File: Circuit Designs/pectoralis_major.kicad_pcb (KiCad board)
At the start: 2 copper layers, 11 x 7.2 mm, 11 parts

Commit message: done all the packages and migrations. Now, time to start to route the module
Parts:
- removed REF** (x3): R-0402, CoF_Resistor:R-0402
- removed REF** (x2): R-0805, CoF_Resistor:R-0805
- removed REF** (x4): C-0402, CoF_Capacitor:C-0402
- removed REF** (x2): C-0805, CoF_Capacitor:C-0805
- added C1: 22uF, CoF_Capacitor:C-0805, F.Cu at (109.1, 60.8)
- added C10: 22uF, CoF_Capacitor:C-0805, F.Cu at (128.1, 49.6)
- added C100: 1uF, CoF_Capacitor:C-0402, F.Cu at (83.8, 33.8)
- added C101: 1uF, CoF_Capacitor:C-0402, F.Cu at (78.4, 40.0)
- added C102: 1uF, CoF_Capacitor:C-0402, F.Cu at (96.5, 22.1)
- added C103: 1uF, CoF_Capacitor:C-0402, F.Cu at (99.2, 20.3)
- added C104: 1uF, CoF_Capacitor:C-0402, F.Cu at (75.7, 43.6)
- added C105: 100nF, CoF_Capacitor:C-0402, F.Cu at (86.5, 33.8)
- added C106: 100nF, CoF_Capacitor:C-0402, F.Cu at (85.6, 30.2)
- added C107: 100nF, CoF_Capacitor:C-0402, F.Cu at (85.6, 28.4)
- added C108: 100nF, CoF_Capacitor:C-0402, F.Cu at (93.7, 20.3)
- added C109: 100pF, CoF_Capacitor:C-0402, F.Cu at (83.0, 24.7)
- added C11: 22uF, CoF_Capacitor:C-0805, F.Cu at (117.5, 60.8)
- added C110: 100nF, CoF_Capacitor:C-0402, F.Cu at (95.0, 25.8)
- added C111: 100pF, CoF_Capacitor:C-0402, F.Cu at (76.0, 27.2)
- added C112: 100pF, CoF_Capacitor:C-0402, F.Cu at (85.6, 20.3)
- added C113: 100pF, CoF_Capacitor:C-0402, F.Cu at (74.8, 30.9)
- added C114: 22uF, CoF_Capacitor:C-0805, F.Cu at (75.3, 63.5)
- added C115: 22uF, CoF_Capacitor:C-0805, F.Cu at (75.3, 60.8)
- added C116: 22uF, CoF_Capacitor:C-0805, F.Cu at (88.3, 49.6)
- added C117: 22uF, CoF_Capacitor:C-0805, F.Cu at (82.7, 54.9)
- added C118: 22uF, CoF_Capacitor:C-0805, F.Cu at (69.9, 66.7)
- added C119: 22uF, CoF_Capacitor:C-0805, F.Cu at (84.1, 52.2)
- added C12: 22uF, CoF_Capacitor:C-0805, F.Cu at (113.1, 66.0)
- added C120: 22uF, CoF_Capacitor:C-0805, F.Cu at (71.1, 63.4)
- added C121: 22uF, CoF_Capacitor:C-0805, F.Cu at (78.5, 54.9)
- added C122: 22uF, CoF_Capacitor:C-0805, F.Cu at (84.1, 49.6)
- added C123: 22uF, CoF_Capacitor:C-0805, F.Cu at (65.7, 68.7)
- added C124: 22uF, CoF_Capacitor:C-0805, F.Cu at (74.2, 58.2)
- added C125: 22uF, CoF_Capacitor:C-0805, F.Cu at (79.9, 49.6)
- added C126: 22uF, CoF_Capacitor:C-0805, F.Cu at (88.3, 52.2)
- added C127: 22uF, CoF_Capacitor:C-0805, F.Cu at (61.5, 69.0)
- added C128: 22uF, CoF_Capacitor:C-0805, F.Cu at (74.2, 53.0)
- added C129: 22uF, CoF_Capacitor:C-0805, F.Cu at (70.0, 55.2)
- added C13: 22uF, CoF_Capacitor:C-0805, F.Cu at (124.0, 54.9)
- added C130: 22uF, CoF_Capacitor:C-0805, F.Cu at (62.6, 66.0)
- added C131: 22uF, CoF_Capacitor:C-0805, F.Cu at (70.0, 52.5)
- added C132: 22uF, CoF_Capacitor:C-0805, F.Cu at (70.0, 57.8)
- added C133: 22uF, CoF_Capacitor:C-0805, F.Cu at (67.9, 60.8)
- added C134: 22uF, CoF_Capacitor:C-0805, F.Cu at (66.8, 64.1)
- added C135: 22uF, CoF_Capacitor:C-0805, F.Cu at (79.9, 52.2)
- added C136: 22uF, CoF_Capacitor:C-0805, F.Cu at (78.5, 57.5)
- added C137: 22uF, CoF_Capacitor:C-0805, F.Cu at (74.2, 55.6)
- added C138: 100nF, CoF_Capacitor:C-0402, F.Cu at (84.2, 60.7)
- added C139: 1uF, CoF_Capacitor:C-0402, F.Cu at (75.8, 69.3)
- added C14: 22uF, CoF_Capacitor:C-0805, F.Cu at (128.1, 52.2)
- added C140: 100nF, CoF_Capacitor:C-0402, F.Cu at (84.6, 58.9)
- added C141: 1uF, CoF_Capacitor:C-0402, F.Cu at (91.8, 51.0)
- added C142: 100nF, CoF_Capacitor:C-0402, F.Cu at (78.8, 61.5)
- added C143: 1uF, CoF_Capacitor:C-0402, F.Cu at (86.1, 54.5)
- added C144: 1uF, CoF_Capacitor:C-0402, F.Cu at (91.8, 52.9)
- added C145: 100nF, CoF_Capacitor:C-0402, F.Cu at (87.4, 56.3)
- added C146: 1uF, CoF_Capacitor:C-0402, F.Cu at (70.4, 70.8)
- added C147: 100nF, CoF_Capacitor:C-0402, F.Cu at (84.6, 57.1)
- added C148: 1uF, CoF_Capacitor:C-0402, F.Cu at (64.9, 70.9)
- added C149: 100nF, CoF_Capacitor:C-0402, F.Cu at (62.8, 63.7)
- added C15: 22uF, CoF_Capacitor:C-0805, F.Cu at (117.3, 63.4)
- added C150: 1nF, CoF_Capacitor:C-0402, F.Cu at (81.5, 62.5)
- added C151: 1nF, CoF_Capacitor:C-0402, F.Cu at (76.1, 65.7)
- added C152: 1nF, CoF_Capacitor:C-0402, F.Cu at (66.1, 66.3)
- added C153: 100nF, CoF_Capacitor:C-0402, F.Cu at (78.8, 67.0)
- added C154: 1uF, CoF_Capacitor:C-0402, F.Cu at (148.9, 48.0)
- added C155: 1uF, CoF_Capacitor:C-0402, F.Cu at (143.6, 54.3)
- added C156: 100nF, CoF_Capacitor:C-0402, F.Cu at (140.8, 56.1)
- added C157: 100nF, CoF_Capacitor:C-0402, F.Cu at (146.3, 52.5)
- added C16: 22uF, CoF_Capacitor:C-0805, F.Cu at (132.3, 49.6)
- added C17: 22uF, CoF_Capacitor:C-0805, F.Cu at (124.0, 57.5)
- added C18: 22uF, CoF_Capacitor:C-0805, F.Cu at (121.8, 60.1)
- added C19: 22uF, CoF_Capacitor:C-0805, F.Cu at (117.3, 66.0)
- added C2: 22uF, CoF_Capacitor:C-0805, F.Cu at (108.9, 63.5)
- added C20: 22uF, CoF_Capacitor:C-0805, F.Cu at (128.2, 54.9)
- added C21: 1uF, CoF_Capacitor:C-0402, F.Cu at (131.6, 51.9)
- added C22: 1uF, CoF_Capacitor:C-0402, F.Cu at (121.0, 62.3)
- added C23: 1uF, CoF_Capacitor:C-0402, F.Cu at (127.4, 57.1)
- added C24: 1uF, CoF_Capacitor:C-0402, F.Cu at (125.2, 59.7)
- added C25: 1uF, CoF_Capacitor:C-0402, F.Cu at (120.8, 64.2)
- added C26: 1uF, CoF_Capacitor:C-0402, F.Cu at (123.7, 62.3)
- added C27: 1uF, CoF_Capacitor:C-0402, F.Cu at (154.7, 23.9)
- added C28: 1uF, CoF_Capacitor:C-0402, F.Cu at (156.9, 22.1)
- added C29: 1uF, CoF_Capacitor:C-0402, F.Cu at (159.6, 20.3)
- added C3: 22uF, CoF_Capacitor:C-0805, F.Cu at (118.5, 53.5)
- added C30: 1uF, CoF_Capacitor:C-0402, F.Cu at (154.7, 25.8)
- added C31: 1uF, CoF_Capacitor:C-0402, F.Cu at (157.4, 23.9)
- added C32: 1uF, CoF_Capacitor:C-0402, F.Cu at (159.6, 22.1)
- added C33: 100nF, CoF_Capacitor:C-0402, F.Cu at (156.9, 20.3)
- added C34: 100nF, CoF_Capacitor:C-0402, F.Cu at (136.0, 23.9)
- added C35: 100nF, CoF_Capacitor:C-0402, F.Cu at (122.9, 31.9)
- added C36: 100nF, CoF_Capacitor:C-0402, F.Cu at (126.6, 32.2)
- added C37: 100nF, CoF_Capacitor:C-0402, F.Cu at (126.4, 26.8)
- added C38: 100nF, CoF_Capacitor:C-0402, F.Cu at (130.5, 22.4)
- added C39: 100nF, CoF_Capacitor:C-0402, F.Cu at (113.1, 40.7)
- added C4: 22uF, CoF_Capacitor:C-0805, F.Cu at (123.9, 49.6)
- added C40: 100nF, CoF_Capacitor:C-0402, F.Cu at (130.5, 24.3)
- added C41: 100nF, CoF_Capacitor:C-0402, F.Cu at (126.4, 28.6)
- added C42: 100nF, CoF_Capacitor:C-0402, F.Cu at (121.1, 34.1)
- added C43: 100nF, CoF_Capacitor:C-0402, F.Cu at (116.6, 38.5)
- added C44: 100nF, CoF_Capacitor:C-0402, F.Cu at (134.3, 20.3)
- added C45: 100nF, CoF_Capacitor:C-0402, F.Cu at (129.1, 26.8)
- added C46: 100nF, CoF_Capacitor:C-0402, F.Cu at (133.2, 22.4)
- added C47: 100nF, CoF_Capacitor:C-0402, F.Cu at (120.4, 36.4)
- added C48: 100nF, CoF_Capacitor:C-0402, F.Cu at (126.4, 30.4)
- added C49: 100nF, CoF_Capacitor:C-0402, F.Cu at (115.8, 40.7)
- added C5: 22uF, CoF_Capacitor:C-0805, F.Cu at (113.3, 60.8)
- added C50: 100nF, CoF_Capacitor:C-0402, F.Cu at (123.9, 33.8)
- added C51: 100nF, CoF_Capacitor:C-0402, F.Cu at (133.2, 24.3)
- added C52: 100nF, CoF_Capacitor:C-0402, F.Cu at (141.4, 22.1)
- added C53: 2.2uF, CoF_Capacitor:C-0402, F.Cu at (128.5, 35.9)
- added C54: 2.2uF, CoF_Capacitor:C-0402, F.Cu at (132.0, 31.6)
- added C55: 100nF, CoF_Capacitor:C-0402, F.Cu at (129.3, 34.0)
- added C56: 1uF, CoF_Capacitor:C-0402, F.Cu at (78.7, 27.2)
- added C57: 1uF, CoF_Capacitor:C-0402, F.Cu at (66.0, 40.1)
- added C58: 100nF, CoF_Capacitor:C-0402, F.Cu at (75.7, 41.8)
- added C59: 10nF, CoF_Capacitor:C-0402, F.Cu at (85.6, 32.0)
- added C6: 22uF, CoF_Capacitor:C-0805, F.Cu at (108.9, 66.2)
- added C60: 1uF, CoF_Capacitor:C-0402, F.Cu at (68.7, 39.6)
- added C61: 1uF, CoF_Capacitor:C-0402, F.Cu at (81.5, 26.6)
- added C62: 100nF, CoF_Capacitor:C-0402, F.Cu at (81.1, 34.5)
- added C63: 10nF, CoF_Capacitor:C-0402, F.Cu at (93.7, 22.1)
- added C64: 1uF, CoF_Capacitor:C-0402, F.Cu at (70.2, 41.4)
- added C65: 1uF, CoF_Capacitor:C-0402, F.Cu at (75.7, 36.3)
- added C66: 100nF, CoF_Capacitor:C-0402, F.Cu at (81.1, 36.3)
- added C67: 10nF, CoF_Capacitor:C-0402, F.Cu at (93.8, 23.9)
- added C68: 1uF, CoF_Capacitor:C-0402, F.Cu at (73.0, 40.0)
- added C69: 1uF, CoF_Capacitor:C-0402, F.Cu at (78.4, 36.3)
- added C7: 22uF, CoF_Capacitor:C-0805, F.Cu at (119.7, 56.1)
- added C70: 100nF, CoF_Capacitor:C-0402, F.Cu at (82.9, 32.0)
- added C71: 10nF, CoF_Capacitor:C-0402, F.Cu at (89.6, 25.8)
- added C72: 1uF, CoF_Capacitor:C-0402, F.Cu at (77.5, 32.7)
- added C73: 1uF, CoF_Capacitor:C-0402, F.Cu at (75.7, 34.5)
- added C74: 1uF, CoF_Capacitor:C-0402, F.Cu at (86.9, 25.8)
- added C75: 1uF, CoF_Capacitor:C-0402, F.Cu at (88.4, 23.9)
- added C76: 1uF, CoF_Capacitor:C-0402, F.Cu at (85.7, 23.9)
- added C77: 1uF, CoF_Capacitor:C-0402, F.Cu at (88.3, 22.1)
- added C78: 1uF, CoF_Capacitor:C-0402, F.Cu at (73.0, 41.8)
- added C79: 1uF, CoF_Capacitor:C-0402, F.Cu at (91.1, 23.9)
- added C8: 22uF, CoF_Capacitor:C-0805, F.Cu at (123.9, 52.2)
- added C80: 22uF, CoF_Capacitor:C-0805, F.Cu at (67.1, 31.9)
- added C81: 22uF, CoF_Capacitor:C-0805, F.Cu at (61.3, 43.9)
- added C82: 22uF, CoF_Capacitor:C-0805, F.Cu at (71.3, 29.3)
- added C83: 22uF, CoF_Capacitor:C-0805, F.Cu at (71.3, 31.9)
- added C84: 22uF, CoF_Capacitor:C-0805, F.Cu at (66.8, 36.0)
- added C85: 22uF, CoF_Capacitor:C-0805, F.Cu at (82.1, 20.7)
- added C86: 22uF, CoF_Capacitor:C-0805, F.Cu at (67.1, 29.3)
- added C87: 22uF, CoF_Capacitor:C-0805, F.Cu at (76.8, 25.0)
- added C88: 22uF, CoF_Capacitor:C-0805, F.Cu at (57.1, 43.9)
- added C89: 6.8pF, CoF_Capacitor:C-0402, F.Cu at (81.4, 22.9)
- added C9: 22uF, CoF_Capacitor:C-0805, F.Cu at (113.1, 63.4)
- added C90: 6.8nF, CoF_Capacitor:C-0402, F.Cu at (64.8, 43.5)
- added C91: 100nF, CoF_Capacitor:C-0402, F.Cu at (92.3, 25.8)
- added C92: 10nF, CoF_Capacitor:C-0402, F.Cu at (77.5, 29.0)
- added C93: 1uF, CoF_Capacitor:C-0402, F.Cu at (88.3, 29.4)
- added C94: 1uF, CoF_Capacitor:C-0402, F.Cu at (96.5, 23.9)
- added C95: 1uF, CoF_Capacitor:C-0402, F.Cu at (91.1, 29.4)
- added C96: 1uF, CoF_Capacitor:C-0402, F.Cu at (88.3, 27.6)
- added C97: 10nF, CoF_Capacitor:C-0402, F.Cu at (83.8, 35.7)
- added C98: 10nF, CoF_Capacitor:C-0402, F.Cu at (88.3, 31.2)
- added C99: 100nF, CoF_Capacitor:C-0402, F.Cu at (78.4, 41.8)
- added D1: LED_A, CoF_Diode:LED-0603, F.Cu at (113.5, 38.7)
- added D10: LED_R, CoF_Diode:LED-0603, F.Cu at (114.6, 36.6)
- added D11: LED_A, CoF_Diode:LED-0603, F.Cu at (127.7, 20.5)
- added D12: LED_R, CoF_Diode:LED-0603, F.Cu at (124.3, 20.5)
- added D13: LED_A, CoF_Diode:LED-0603, F.Cu at (110.0, 38.4)
- added D14: LED_R, CoF_Diode:LED-0603, F.Cu at (123.3, 30.0)
- added D15: LED_A, CoF_Diode:LED-0603, F.Cu at (119.8, 27.8)
- added D16: LED_R, CoF_Diode:LED-0603, F.Cu at (124.0, 23.6)
- added D17: LED_A, CoF_Diode:LED-0603, F.Cu at (114.6, 34.4)
- added D18: B5819W, CoF_Diode:SOD-123, F.Cu at (67.6, 20.9)
- added D2: LED_R, CoF_Diode:LED-0603, F.Cu at (131.2, 20.5)
- added D3: LED_A, CoF_Diode:LED-0603, F.Cu at (127.4, 24.8)
- added D4: LED_R, CoF_Diode:LED-0603, F.Cu at (119.8, 32.1)
- added D5: LED_A, CoF_Diode:LED-0603, F.Cu at (118.1, 34.4)
- added D6: LED_R, CoF_Diode:LED-0603, F.Cu at (119.8, 30.0)
- added D7: LED_A, CoF_Diode:LED-0603, F.Cu at (123.3, 27.8)
- added D8: LED_R, CoF_Diode:LED-0603, F.Cu at (110.0, 40.6)
- added D9: LED_A, CoF_Diode:LED-0603, F.Cu at (127.4, 22.6)
- added J1: 0524651671, CoF_Connector:524651671, F.Cu at (104.5, 51.6)
- added J2: 0533071071, CoF_Connector:0533071071, F.Cu at (103.4, 58.5)
- added J3: 0533071071, CoF_Connector:0533071071, F.Cu at (112.8, 52.0)
- added J4: 0524651071, CoF_Connector:524651071, F.Cu at (103.3, 65.5)
- added J5: SoicBite, CoF_Connector:SoicBite, F.Cu at (108.5, 36.4)
- added L1: 22uH, CoF_Inductor:L-7.1-6.6, F.Cu at (59.8, 38.7)
- added Q1: AO3400A, CoF_SmallOutline:SOT-23, F.Cu at (120.1, 24.7)
- added Q2: AO3400A, CoF_SmallOutline:SOT-23, F.Cu at (106.2, 39.5)
- added Q3: BUK7V4R2, CoF_SmallOutline:SOT-1205, F.Cu at (58.2, 60.3)
- added Q4: BUK7V4R2, CoF_SmallOutline:SOT-1205, F.Cu at (64.7, 52.1)
- added Q5: BUK7V4R2, CoF_SmallOutline:SOT-1205, F.Cu at (58.2, 52.1)
- added R1: 22R, CoF_Resistor:R-0402, F.Cu at (151.9, 24.5)
- added R10: 10K, CoF_Resistor:R-0402, F.Cu at (129.3, 32.2)
- added R11: 100R, CoF_Resistor:R-0402, F.Cu at (137.2, 25.8)
- added R12: 22R, CoF_Resistor:R-0402, F.Cu at (131.8, 29.7)
- added R13: 22R, CoF_Resistor:R-0402, F.Cu at (125.8, 35.9)
- added R14: 10K, CoF_Resistor:R-0402, F.Cu at (122.0, 38.2)
- added R15: 3.3K, CoF_Resistor:R-0402, F.Cu at (138.7, 23.9)
- added R16: 3.3K, CoF_Resistor:R-0402, F.Cu at (134.5, 27.9)
- added R17: 2.2K, CoF_Resistor:R-0402, F.Cu at (136.0, 22.1)
- added R18: 2.2K, CoF_Resistor:R-0402, F.Cu at (123.1, 35.9)
- added R19: 1K, CoF_Resistor:R-0402, F.Cu at (129.1, 28.6)
- added R2: 22R, CoF_Resistor:R-0402, F.Cu at (149.2, 26.3)
- added R20: 1K, CoF_Resistor:R-0402, F.Cu at (137.0, 20.3)
- added R21: 680R, CoF_Resistor:R-0402, F.Cu at (138.7, 22.1)
- added R22: 680R, CoF_Resistor:R-0402, F.Cu at (126.6, 34.0)
- added R23: 470R, CoF_Resistor:R-0402, F.Cu at (122.0, 40.0)
- added R24: 680R, CoF_Resistor:R-0402, F.Cu at (134.5, 26.1)
- added R25: 680R, CoF_Resistor:R-0402, F.Cu at (139.7, 20.3)
- added R26: 1K, CoF_Resistor:R-0402, F.Cu at (119.3, 38.2)
- added R27: 1K, CoF_Resistor:R-0402, F.Cu at (131.8, 26.1)
- added R28: 2.2K, CoF_Resistor:R-0402, F.Cu at (119.3, 40.0)
- added R29: 2.2K, CoF_Resistor:R-0402, F.Cu at (129.1, 30.4)
- added R3: 1K, CoF_Resistor:R-0402, F.Cu at (151.9, 26.3)
- added R30: 3.3K, CoF_Resistor:R-0402, F.Cu at (124.7, 37.7)
- added R31: 3.3K, CoF_Resistor:R-0402, F.Cu at (142.5, 20.3)
- added R32: 470R, CoF_Resistor:R-0402, F.Cu at (124.7, 39.5)
- added R33: 470R, CoF_Resistor:R-0402, F.Cu at (134.5, 29.7)
- added R34: 10K, CoF_Resistor:R-0402, F.Cu at (117.7, 36.4)
- added R35: 10K, CoF_Resistor:R-0402, F.Cu at (123.6, 25.6)
- added R36: 0R, CoF_Resistor:R-0402, F.Cu at (91.0, 22.1)
- added R37: 10K, CoF_Resistor:R-0402, F.Cu at (66.0, 38.3)
- added R38: 0R, CoF_Resistor:R-0402, F.Cu at (77.5, 30.9)
- added R39: 18K, CoF_Resistor:R-0402, F.Cu at (73.0, 36.3)
- added R4: 10K, CoF_Resistor:R-0402, F.Cu at (149.2, 24.5)
- added R40: 0R, CoF_Resistor:R-0402, F.Cu at (91.0, 20.3)
- added R41: 10K, CoF_Resistor:R-0402, F.Cu at (73.0, 38.1)
- added R42: 0R, CoF_Resistor:R-0402, F.Cu at (75.7, 38.1)
- added R43: 10K, CoF_Resistor:R-0402, F.Cu at (81.1, 38.1)
- added R44: 2.2K, CoF_Resistor:R-0402, F.Cu at (70.2, 34.1)
- added R45: 3.3K, CoF_Resistor:R-0402, F.Cu at (67.5, 41.9)
- added R46: 2.2K, CoF_Resistor:R-0402, F.Cu at (80.2, 30.9)
- added R47: 4.7K, CoF_Resistor:R-0402, F.Cu at (91.1, 27.6)
- added R48: 1K, CoF_Resistor:R-0402, F.Cu at (74.8, 29.0)
- added R49: 100R, CoF_Resistor:R-0402, F.Cu at (84.2, 26.6)
- added R5: 10K, CoF_Resistor:R-0402, F.Cu at (154.2, 20.3)
- added R50: 1K, CoF_Resistor:R-0402, F.Cu at (82.9, 28.4)
- added R51: 680R, CoF_Resistor:R-0402, F.Cu at (67.5, 43.7)
- added R52: 18K, CoF_Resistor:R-0402, F.Cu at (80.2, 32.7)
- added R53: 3.3K, CoF_Resistor:R-0402, F.Cu at (78.4, 34.5)
- added R54: 100K, CoF_Resistor:R-0402, F.Cu at (70.2, 37.8)
- added R55: 200K, CoF_Resistor:R-0402, F.Cu at (88.3, 20.3)
- added R56: 10K, CoF_Resistor:R-0402, F.Cu at (70.2, 43.2)
- added R57: 10K, CoF_Resistor:R-0402, F.Cu at (82.9, 30.2)
- added R58: 10K, CoF_Resistor:R-0402, F.Cu at (74.8, 32.7)
- added R59: 2.2K, CoF_Resistor:R-0402, F.Cu at (85.6, 22.1)
- added R6: 3.3K, CoF_Resistor:R-0402, F.Cu at (162.3, 20.3)
- added R60: 10K, CoF_Resistor:R-0402, F.Cu at (75.7, 40.0)
- added R61: 0R, CoF_Resistor:R-0402, F.Cu at (73.0, 43.6)
- added R62: 10K, CoF_Resistor:R-0402, F.Cu at (80.2, 24.7)
- added R63: 10K, CoF_Resistor:R-0402, F.Cu at (78.4, 38.1)
- added R64: 10K, CoF_Resistor:R-0402, F.Cu at (80.2, 29.0)
- added R65: 2.2K, CoF_Resistor:R-0402, F.Cu at (70.2, 35.9)
- added R66: 2.2K, CoF_Resistor:R-0402, F.Cu at (96.5, 20.3)
- added R67: 2.2K, CoF_Resistor:R-0402, F.Cu at (73.0, 34.5)
- added R68: 1R, CoF_Resistor:R-0402, F.Cu at (94.5, 51.0)
- added R69: 1R, CoF_Resistor:R-0402, F.Cu at (88.9, 54.5)
- added R7: 22R, CoF_Resistor:R-0402, F.Cu at (157.4, 25.8)
- added R70: 1R, CoF_Resistor:R-0402, F.Cu at (81.5, 60.7)
- added R71: 2mR, CoF_Resistor:R-1206, F.Cu at (57.8, 66.2)
- added R72: 2mR, CoF_Resistor:R-1206, F.Cu at (64.2, 58.0)
- added R73: 2mR, CoF_Resistor:R-1206, F.Cu at (70.7, 49.8)
- added R74: 1R, CoF_Resistor:R-0402, F.Cu at (87.4, 58.1)
- added R75: 1R, CoF_Resistor:R-0402, F.Cu at (94.5, 49.2)
- added R76: 1R, CoF_Resistor:R-0402, F.Cu at (73.1, 69.3)
- added R77: 1K, CoF_Resistor:R-0402, F.Cu at (78.8, 65.2)
- added R78: 1K, CoF_Resistor:R-0402, F.Cu at (81.9, 58.9)
- added R79: 1K, CoF_Resistor:R-0402, F.Cu at (78.8, 59.7)
- added R8: 22R, CoF_Resistor:R-0402, F.Cu at (160.1, 23.9)
- added R80: 680R, CoF_Resistor:R-0402, F.Cu at (78.8, 63.4)
- added R81: 680R, CoF_Resistor:R-0402, F.Cu at (73.4, 67.5)
- added R82: 680R, CoF_Resistor:R-0402, F.Cu at (67.7, 70.9)
- added R83: 3.3K, CoF_Resistor:R-0402, F.Cu at (76.1, 67.5)
- added R84: 3.3K, CoF_Resistor:R-0402, F.Cu at (91.8, 49.2)
- added R85: 3.3K, CoF_Resistor:R-0402, F.Cu at (81.9, 57.1)
- added R86: 10K, CoF_Resistor:R-0402, F.Cu at (69.2, 68.9)
- added R87: 10K, CoF_Resistor:R-0402, F.Cu at (140.8, 54.3)
- added R88: 10K, CoF_Resistor:R-0402, F.Cu at (148.9, 46.2)
- added R89: 10K, CoF_Resistor:R-0402, F.Cu at (140.8, 52.5)
- added R9: 100R, CoF_Resistor:R-0402, F.Cu at (154.2, 22.1)
- added R90: 10K, CoF_Resistor:R-0402, F.Cu at (143.6, 52.5)
- added SP1: A, CoF_Connector:SolderPt_2.5x4mm, F.Cu at (115.0, 57.6)
- added SP2: B, CoF_Connector:SolderPt_2.5x4mm, F.Cu at (119.1, 50.2)
- added SP3: C, CoF_Connector:SolderPt_2.5x4mm, F.Cu at (109.6, 57.6)
- added T1: B3380, CoF_Resistor:R-0402, F.Cu at (131.8, 27.9)
- added T2: B3380, CoF_Resistor:R-0402, F.Cu at (73.4, 65.7)
- added U1: TCAN330, CoF_SmallOutline:TSOT-23-8, F.Cu at (150.3, 21.5)
- added U10: INA199A1, CoF_SmallOutline:SOT-363, F.Cu at (57.2, 69.4)
- added U11: AS5047P, CoF_SmallOutline:TSSOP-14, F.Cu at (143.5, 48.4)
- added U2: STM32F405RGTx, CoF_QuadFlat:LQFP-64, F.Cu at (111.1, 26.4)
- added U3: AP2127, CoF_SmallOutline:SOT-23-5, F.Cu at (72.2, 25.8)
- added U4: AP2127, CoF_SmallOutline:SOT-23-5, F.Cu at (67.4, 25.8)
- added U5: AP2127, CoF_SmallOutline:SOT-23-5, F.Cu at (77.6, 21.6)
- added U6: AP2127, CoF_SmallOutline:SOT-23-5, F.Cu at (72.7, 21.6)
- added U7: DRV8301, CoF_SmallOutline:HTSSOP-56-EP, F.Cu at (60.0, 27.2)
- added U8: INA199A1, CoF_SmallOutline:SOT-363, F.Cu at (75.6, 50.0)
- added U9: INA199A1, CoF_SmallOutline:SOT-363, F.Cu at (63.6, 61.2)
- added Y1: CSTNE8M00, CoF_Crystal:CSTNE, F.Cu at (120.3, 21.0)
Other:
- board size 11 x 7.2 mm -> 100 x 100 mm

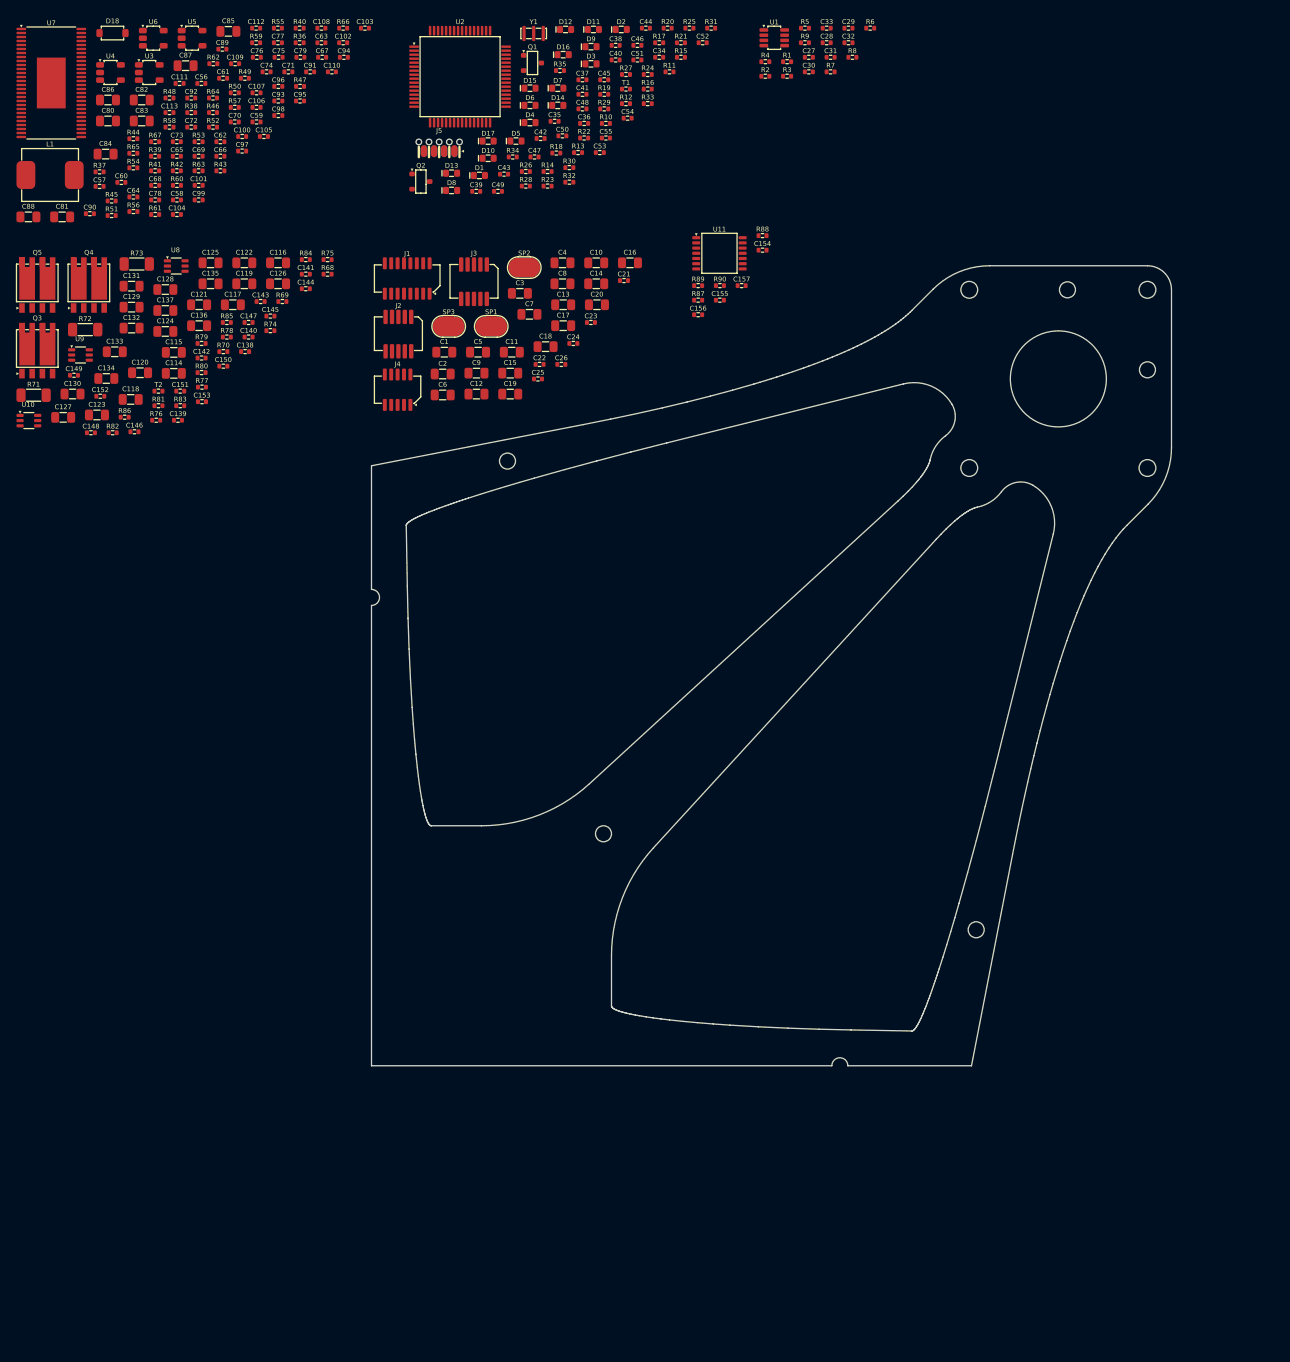
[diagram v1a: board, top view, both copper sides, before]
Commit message: placed LEDs, mosfets, bulk capacitors
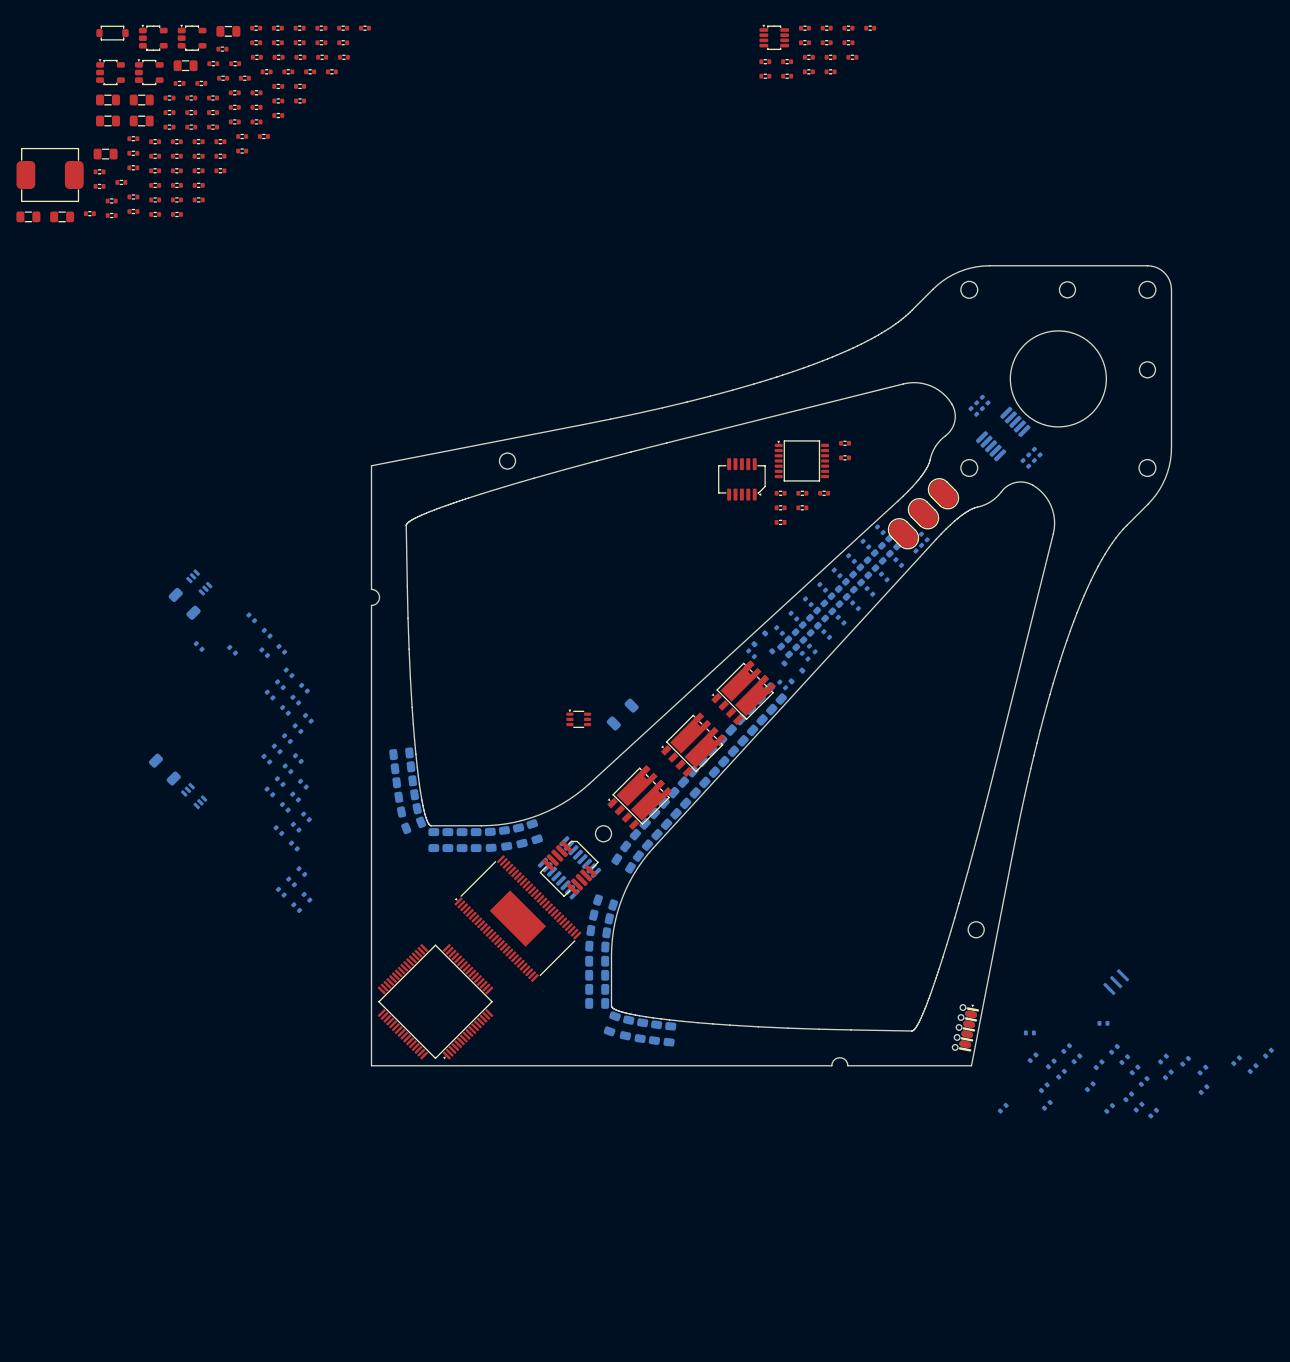
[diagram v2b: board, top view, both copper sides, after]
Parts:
- C1, C10, C11, C114, C115, C116, C117, C118, C119, C12, C120, C121, C122, C123, C124, C125, C126, C127, C128, C129, C13, C130, C131, C132, C133, C134, C135, C136, C137, C138, C139, C14, C140, C141, C142, C143, C144, C145, C146, C147, C148, C149, C15, C150, C151, C152, C153, C16, C17, C18, C19, C2, C20, C21, C22, C23, C24, C25, C26, C3, C34, C35, C36, C37, C38, C39, C4, C40, C41, C42, C43, C44, C45, C46, C47, C48, C49, C5, C50, C51, C52, C53, C54, C55, C6, C7, C8, C9, D1, D10, D11, D12, D13, D14, D15, D16, D17, D2, D3, D4, D5, D6, D7, D8, D9, J1, J3, Q1, Q2, R10, R11, R12, R13, R14, R15, R16, R17, R18, R19, R20, R21, R22, R23, R24, R25, R26, R27, R28, R29, R30, R31, R32, R33, R34, R35, R68, R69, R70, R71, R72, R73, R74, R75, R76, R77, R78, R79, R80, R81, R82, R83, R84, R85, R86, T1, T2, U10, U8, Y1: moved to B.Cu
- moved C39 146.3 mm to (212.1, 148.4), turned to -135 degrees
- moved C49 144.7 mm to (210.2, 150.4), turned to -135 degrees
- moved C43 143.8 mm to (208.1, 149.4), turned to -135 degrees
- moved C47 141.5 mm to (203.9, 150.5), turned to -135 degrees
- moved R14 141.1 mm to (204.1, 153.0), turned to -135 degrees
- moved C42 140.7 mm to (201.8, 149.4), turned to -135 degrees
- moved C35 139.8 mm to (199.0, 149.2), turned to -135 degrees
- moved C50 139.7 mm to (199.6, 151.1), turned to -135 degrees
- moved Y1 139.2 mm to (193.1, 139.5), turned to -135 degrees
- moved C36 138.7 mm to (196.6, 152.0), turned to -135 degrees
- moved C53 138.6 mm to (197.8, 155.9), turned to -135 degrees
- moved C48 138.6 mm to (195.4, 150.5), turned to -135 degrees
- moved C41 138.4 mm to (194.2, 149.2), turned to -135 degrees
- moved C52 138.4 mm to (179.0, 155.3), turned to -135 degrees
- moved C55 138.3 mm to (195.9, 155.2), turned to -135 degrees
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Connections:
- Q3 pad 6: Net-(Q3-Pad6) -> /powerDrivers/SH_A
- Q4 pad 6: Net-(Q4-Pad6) -> /powerDrivers/SH_B
- Q5 pad 6: Net-(Q5-Pad6) -> /powerDrivers/SH_C
- R71 pad 1: Net-(Q3-Pad6) -> /powerDrivers/SH_A
- R72 pad 1: Net-(Q4-Pad6) -> /powerDrivers/SH_B
- R73 pad 1: Net-(Q5-Pad6) -> /powerDrivers/SH_C

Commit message: placed current shunt circuits and mosfets
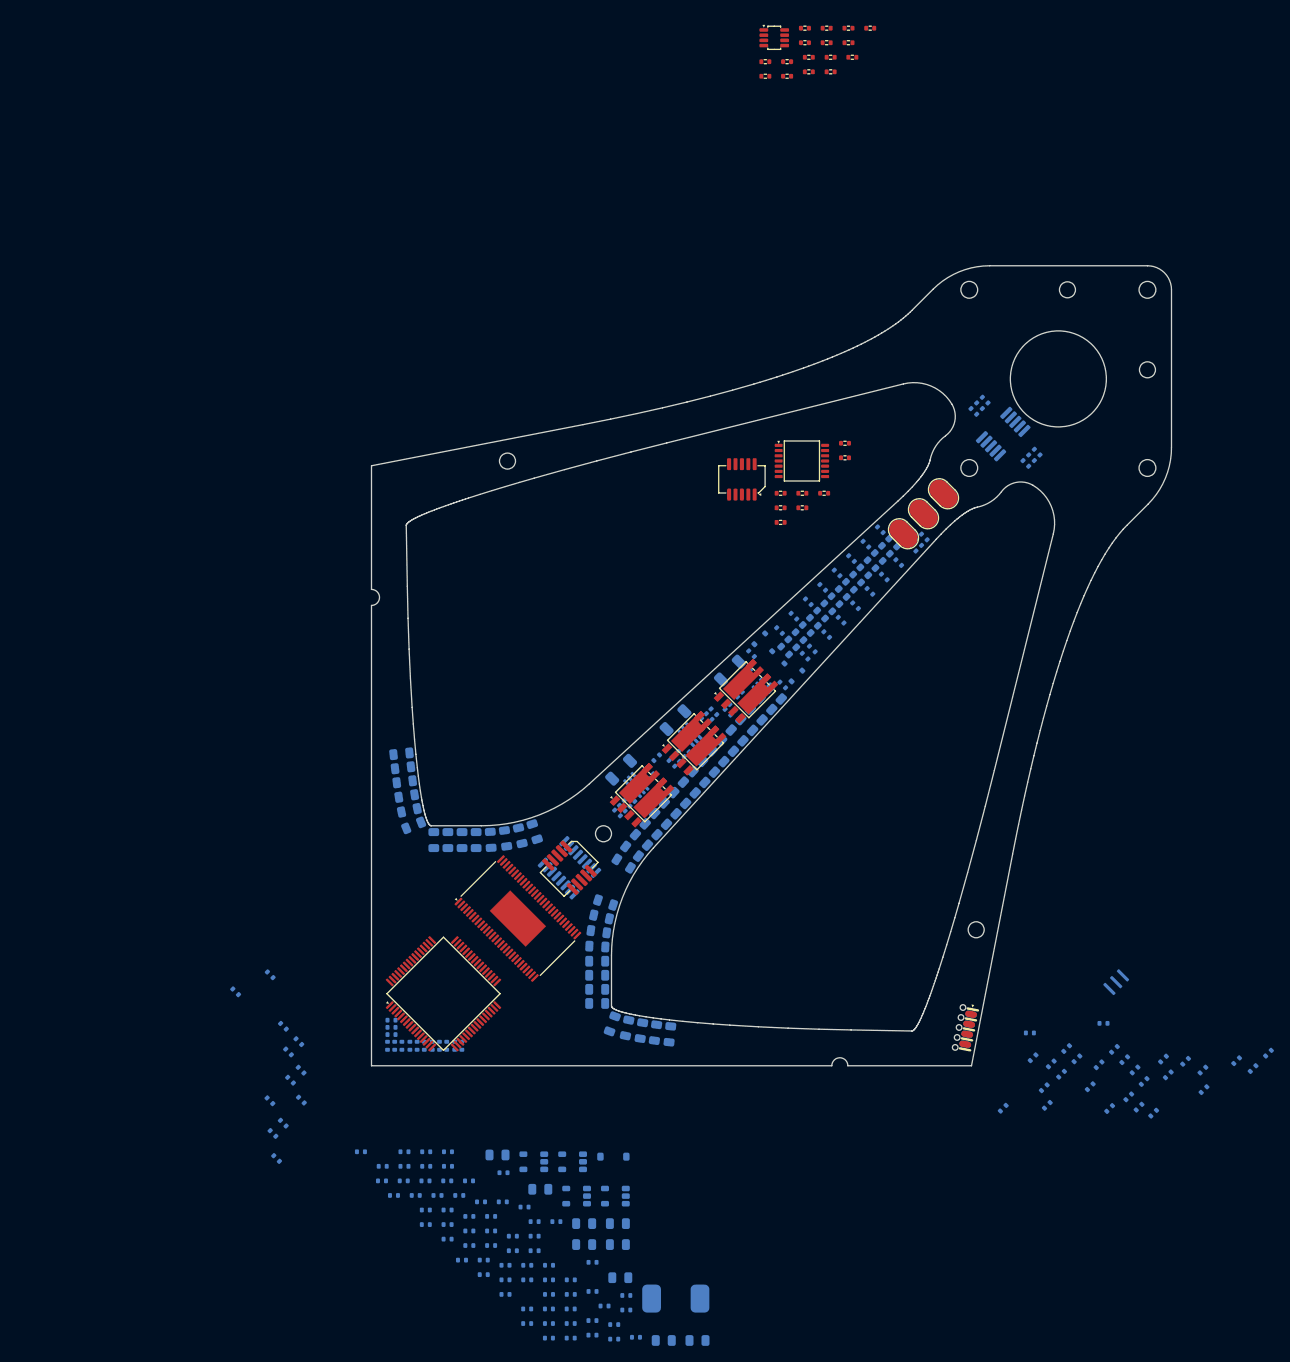
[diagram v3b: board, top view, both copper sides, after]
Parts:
- C100, C101, C102, C103, C104, C105, C106, C107, C108, C109, C110, C111, C112, C113, C56, C57, C58, C59, C60, C61, C62, C63, C64, C65, C66, C67, C68, C69, C70, C71, C72, C73, C74, C75, C76, C77, C78, C79, C80, C81, C82, C83, C84, C85, C86, C87, C88, C89, C90, C91, C92, C93, C94, C95, C96, C97, C98, C99, D18, L1, R36, R37, R38, R39, R40, R41, R42, R43, R44, R45, R46, R47, R48, R49, R50, R51, R52, R53, R54, R55, R56, R57, R58, R59, R60, R61, R62, R63, R64, R65, R66, R67, U3, U4, U5, U6, U9: moved to B.Cu
- moved C88 163.5 mm to (140.8, 184.3), turned to 180 degrees
- moved L1 160.8 mm to (138.0, 179.1), turned to 180 degrees
- moved C81 159.3 mm to (136.5, 184.3), turned to 180 degrees
- moved C90 156.2 mm to (133.1, 183.9), turned to 180 degrees
- moved R37 155.1 mm to (131.8, 178.7), turned to 180 degrees
- moved C57 155.1 mm to (131.8, 180.5), turned to 180 degrees
- moved C84 154.5 mm to (131.1, 176.5), turned to 180 degrees
- moved C80 154.2 mm to (130.8, 172.3), turned to 180 degrees
- moved C86 154.2 mm to (130.8, 169.7), turned to 180 degrees
- moved U4 154.0 mm to (130.5, 166.3), turned to 180 degrees
- moved R45 153.9 mm to (130.3, 182.3), turned to 180 degrees
- moved R51 153.9 mm to (130.3, 184.2), turned to 180 degrees
- moved D18 153.8 mm to (130.2, 161.4), turned to 180 degrees
- moved C60 152.9 mm to (129.1, 180.0), turned to 180 degrees
- moved R54 151.7 mm to (127.6, 178.2), turned to 180 degrees
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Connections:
- U10 pad 4: /powerSemicons/PH_C -> /powerDrivers/SH_C
- U10 pad 5: /powerDrivers/SH_C -> /powerSemicons/PH_C
- U8 pad 4: /powerSemicons/PH_A -> /powerDrivers/SH_A
- U8 pad 5: /powerDrivers/SH_A -> /powerSemicons/PH_A
- U9 pad 4: /powerSemicons/PH_B -> /powerDrivers/SH_B
- U9 pad 5: /powerDrivers/SH_B -> /powerSemicons/PH_B
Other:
- copper layers 2 -> 4
